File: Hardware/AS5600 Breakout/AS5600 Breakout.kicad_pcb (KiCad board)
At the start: 2 copper layers, 42.3 x 42.3 mm, 161 parts, among them J1 Conn_01x08, U1 AS5600

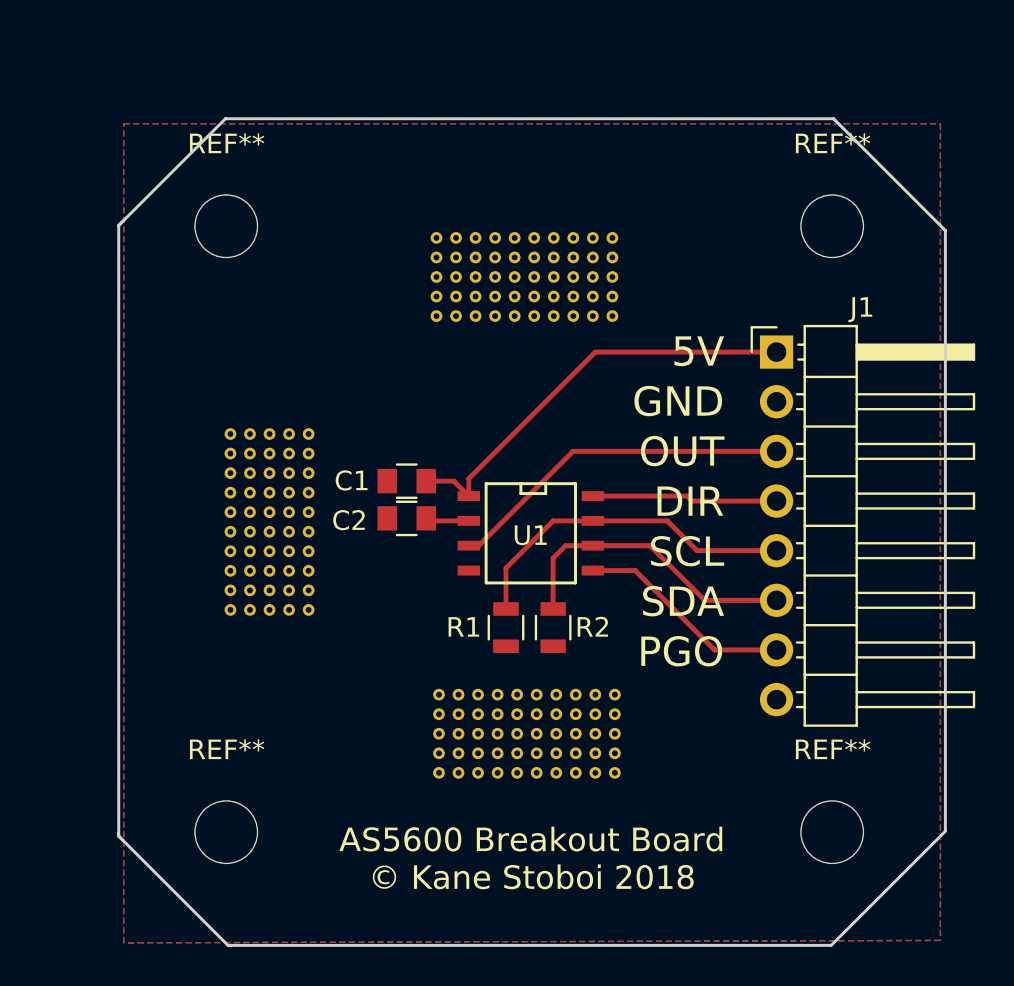
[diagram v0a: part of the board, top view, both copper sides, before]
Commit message: Completed breakout boards and BOM
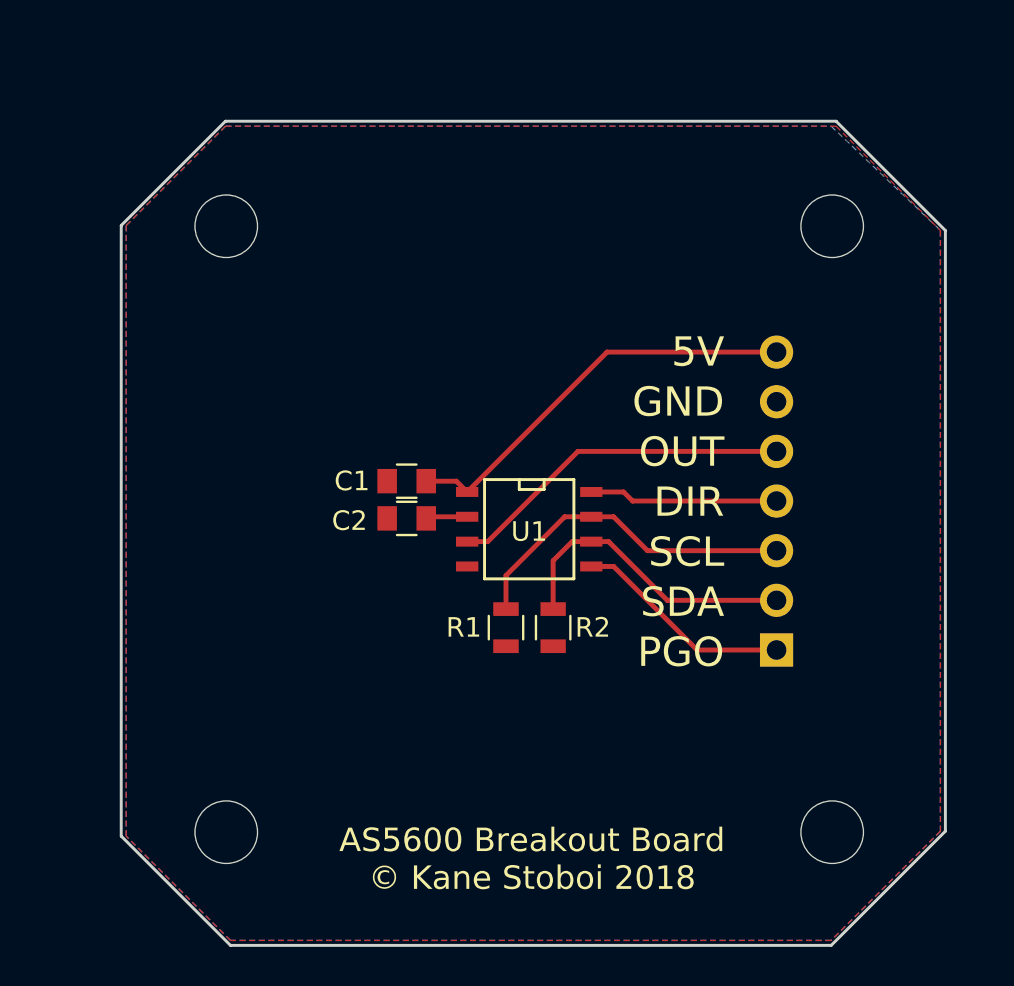
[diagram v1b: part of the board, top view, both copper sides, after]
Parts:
- removed the REF** at (145.4, 128.6)
- removed the REF** at (136.4, 128.6)
- removed the REF** at (144.3, 105.2)
- removed the REF** at (143.3, 105.2)
- removed the REF** at (142.3, 105.2)
- removed the REF** at (141.3, 105.2)
- removed the REF** at (140.3, 105.2)
- removed the REF** at (139.3, 105.2)
- removed the REF** at (138.3, 105.2)
- removed the REF** at (137.3, 105.2)
- removed the REF** at (136.3, 105.2)
- removed the REF** at (145.3, 104.2)
- removed the REF** at (145.4, 127.6)
- removed the REF** at (144.3, 104.2)
- removed the REF** at (143.3, 104.2)
- removed the REF** at (142.3, 104.2)
- removed the REF** at (141.3, 104.2)
- removed the REF** at (140.3, 104.2)
- removed the REF** at (139.3, 104.2)
- removed the REF** at (138.3, 104.2)
- removed the REF** at (137.3, 104.2)
- removed the REF** at (136.3, 104.2)
- removed the REF** at (145.3, 103.2)
- removed the REF** at (144.4, 127.6)
- removed the REF** at (144.3, 103.2)
- removed the REF** at (143.3, 103.2)
- removed the REF** at (142.3, 103.2)
- removed the REF** at (141.3, 103.2)
- removed the REF** at (140.3, 103.2)
- removed the REF** at (139.3, 103.2)
- removed the REF** at (138.3, 103.2)
- removed the REF** at (137.3, 103.2)
- removed the REF** at (136.3, 103.2)
- removed the REF** at (145.3, 102.2)
- removed the REF** at (143.4, 127.6)
- removed the REF** at (144.3, 102.2)
- removed the REF** at (143.3, 102.2)
- removed the REF** at (142.3, 102.2)
- removed the REF** at (141.3, 102.2)
- removed the REF** at (140.3, 102.2)
- removed the REF** at (139.3, 102.2)
- removed the REF** at (138.3, 102.2)
- removed the REF** at (137.3, 102.2)
- removed the REF** at (136.3, 102.2)
- removed the REF** at (145.3, 101.2)
- removed the REF** at (142.4, 127.6)
- removed the REF** at (144.3, 101.2)
- removed the REF** at (143.3, 101.2)
- removed the REF** at (142.3, 101.2)
- removed the REF** at (141.3, 101.2)
- removed the REF** at (140.3, 101.2)
- removed the REF** at (139.3, 101.2)
- removed the REF** at (138.3, 101.2)
- removed the REF** at (137.3, 101.2)
- removed the REF** at (141.4, 127.6)
- removed the REF** at (136.3, 101.2)
- removed the REF** at (125.7, 111.3)
- removed the REF** at (136.4, 124.6)
- removed the REF** at (140.4, 127.6)
- removed the REF** at (139.4, 127.6)
- removed the REF** at (138.4, 127.6)
- removed the REF** at (137.4, 127.6)
- removed the REF** at (144.4, 128.6)
- removed the REF** at (136.4, 127.6)
- removed the REF** at (145.4, 126.6)
- removed the REF** at (144.4, 126.6)
- removed the REF** at (143.4, 126.6)
- removed the REF** at (142.4, 126.6)
- removed the REF** at (141.4, 126.6)
- removed the REF** at (140.4, 126.6)
- removed the REF** at (139.4, 126.6)
- removed the REF** at (138.4, 126.6)
- removed the REF** at (137.4, 126.6)
- removed the REF** at (143.4, 128.6)
- removed the REF** at (136.4, 126.6)
- removed the REF** at (145.4, 125.6)
- removed the REF** at (144.4, 125.6)
- removed the REF** at (143.4, 125.6)
- removed the REF** at (142.4, 125.6)
- removed the REF** at (141.4, 125.6)
- removed the REF** at (140.4, 125.6)
- removed the REF** at (139.4, 125.6)
- removed the REF** at (138.4, 125.6)
- removed the REF** at (137.4, 125.6)
- removed the REF** at (142.4, 128.6)
- removed the REF** at (136.4, 125.6)
- removed the REF** at (145.4, 124.6)
- removed the REF** at (144.4, 124.6)
- removed the REF** at (143.4, 124.6)
- removed the REF** at (142.4, 124.6)
- removed the REF** at (141.4, 124.6)
- removed the REF** at (140.4, 124.6)
- removed the REF** at (139.4, 124.6)
- removed the REF** at (138.4, 124.6)
- removed the REF** at (137.4, 124.6)
- removed the REF** at (141.4, 128.6)
- removed the REF** at (129.7, 120.3)
- removed the REF** at (128.7, 120.3)
- removed the REF** at (127.7, 120.3)
- removed the REF** at (126.7, 120.3)
- removed the REF** at (125.7, 120.3)
- removed the REF** at (129.7, 119.3)
- removed the REF** at (128.7, 119.3)
- removed the REF** at (127.7, 119.3)
- removed the REF** at (126.7, 119.3)
- removed the REF** at (125.7, 119.3)
- removed the REF** at (140.4, 128.6)
- removed the REF** at (129.7, 118.3)
- removed the REF** at (128.7, 118.3)
- removed the REF** at (127.7, 118.3)
- removed the REF** at (126.7, 118.3)
- removed the REF** at (125.7, 118.3)
- removed the REF** at (129.7, 117.3)
- removed the REF** at (128.7, 117.3)
- removed the REF** at (127.7, 117.3)
- removed the REF** at (126.7, 117.3)
- removed the REF** at (125.7, 117.3)
- removed the REF** at (139.4, 128.6)
- removed the REF** at (129.7, 116.3)
- removed the REF** at (128.7, 116.3)
- removed the REF** at (127.7, 116.3)
- removed the REF** at (126.7, 116.3)
- removed the REF** at (125.7, 116.3)
- removed the REF** at (129.7, 115.3)
- removed the REF** at (128.7, 115.3)
- removed the REF** at (127.7, 115.3)
- removed the REF** at (126.7, 115.3)
- removed the REF** at (125.7, 115.3)
- removed the REF** at (138.4, 128.6)
- removed the REF** at (129.7, 114.3)
- removed the REF** at (128.7, 114.3)
- removed the REF** at (127.7, 114.3)
- removed the REF** at (126.7, 114.3)
- removed the REF** at (125.7, 114.3)
- removed the REF** at (129.7, 113.3)
- removed the REF** at (128.7, 113.3)
- removed the REF** at (127.7, 113.3)
- removed the REF** at (126.7, 113.3)
- removed the REF** at (125.7, 113.3)
- removed the REF** at (137.4, 128.6)
- removed the REF** at (129.7, 112.3)
- removed the REF** at (128.7, 112.3)
- removed the REF** at (127.7, 112.3)
- removed the REF** at (126.7, 112.3)
- removed the REF** at (125.7, 112.3)
- removed the REF** at (129.7, 111.3)
- removed the REF** at (128.7, 111.3)
- removed the REF** at (127.7, 111.3)
- removed the REF** at (126.7, 111.3)
- removed the REF** at (145.3, 105.2)
- ? (x4): renamed from REF**; value MountingHole_3.2mm_M3 -> (none)
- J1: value Conn_01x08 -> Conn_01x07; footprint Pin_Headers:Pin_Header_Angled_1x08_Pitch2.54mm -> Pin_Headers:Pin_Header_Angled_1x07_Pitch2.54mm; moved to B.Cu
- moved J1 15.2 mm to (153.7, 122.3)
- moved U1 0.22 mm to (141.0, 116.1)
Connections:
- J1 pad 1: 5V -> PGO
- J1 pad 2: GND -> SDA
- J1 pad 3: OUT -> SCL
- J1 pad 5: SCL -> OUT
- J1 pad 6: SDA -> GND
- J1 pad 7: PGO -> 5V
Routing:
- net 5V: track 21.8 -> 21.1 mm
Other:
- board size 42.3 x 42.3 mm -> 42.2 x 42.2 mm

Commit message: Created gerbers for pcbs
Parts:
- added REF**: VIA-0.6mm, VIAs:VIA-0.6mm, F.Cu at (137.5, 101.3)
- added REF**: VIA-0.6mm, VIAs:VIA-0.6mm, F.Cu at (135.0, 118.0)
- added REF**: VIA-0.6mm, VIAs:VIA-0.6mm, F.Cu at (135.0, 119.6)
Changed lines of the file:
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@@
 (kicad_pcb (version 4) (host pcbnew 4.0.7)
   (general
-    (links 15)
+    (links 18)
     (no_connects 0)
-    (area 120.066999 95.174999 162.381001 137.489001)
+    (area -4.438094 -2.499 164.445001 137.489001)
     (thickness 1.6)
     (drawings 24)
     (tracks 28)
     (zones 0)
-    (modules 11)
+    (modules 14)
     (nets 9)
   )
@@
   (layers
     (0 F.Cu signal)
-    (31 B.Cu signal hide)
+    (31 B.Cu signal)
     (32 B.Adhes user)
     (33 F.Adhes user)
@@
     (visible_elements 7FFEFF7F)
     (pcbplotparams
-      (layerselection 0x00030_80000001)
-      (usegerberextensions false)
+      (layerselection 0x010f0_80000001)
+      (usegerberextensions true)
       (excludeedgelayer true)
       (linewidth 0.100000)
@@
       (psa4output false)
       (plotreference true)
-      (plotvalue true)
+      (plotvalue false)
       (plotinvisibletext false)
       (padsonsilk false)
@@
       (outputformat 1)
       (mirror false)
-      (drillshape 1)
+      (drillshape 0)
       (scaleselection 1)
       (outputdirectory ""))
@@
     (add_net SCL)
     (add_net SDA)
+  )
+  (module VIAs:VIA-0.6mm (layer F.Cu)
+    (at 137.541 101.346)
+    (fp_text reference REF** (at 0 1.397) (layer F.SilkS) hide
+      (effects (font (size 1 1) (thickness 0.15)))
+    )
+    (fp_text value VIA-0.6mm (at 0 -1.524) (layer F.Fab) hide
+      (effects (font (size 1 1) (thickness 0.15)))
+    )
+    (pad 1 thru_hole circle (at 0 0) (size 0.6 0.6) (drill 0.3) (layers *.Cu)
+      (net 1 GND) (zone_connect 2))
+  )
+  (module VIAs:VIA-0.6mm (layer F.Cu)
+    (at 135.001 117.983)
+    (fp_text reference REF** (at 0 1.397) (layer F.SilkS) hide
+      (effects (font (size 1 1) (thickness 0.15)))
+    )
+    (fp_text value VIA-0.6mm (at 0 -1.524) (layer F.Fab) hide
+      (effects (font (size 1 1) (thickness 0.15)))
+    )
+    (pad 1 thru_hole circle (at 0 0) (size 0.6 0.6) (drill 0.3) (layers *.Cu)
+      (net 1 GND) (zone_connect 2))
   )
   (module VIA-0.6mm (layer F.Cu)
@@
     )
   )
+  (module VIAs:VIA-0.6mm (layer F.Cu)
+    (at 135.001 119.634)
+    (fp_text reference REF** (at 0 1.397) (layer F.SilkS) hide
+      (effects (font (size 1 1) (thickness 0.15)))
+    )
+    (fp_text value VIA-0.6mm (at 0 -1.524) (layer F.Fab) hide
+      (effects (font (size 1 1) (thickness 0.15)))
+    )
+    (pad 1 thru_hole circle (at 0 0) (size 0.6 0.6) (drill 0.3) (layers *.Cu)
+      (net 1 GND) (zone_connect 2))
+  )
   (gr_text "AS5600 Breakout Board\n© Kane Stoboi 2018" (at 141.165 133) (layer B.SilkS)
     (effects (font (size 1.2 1.2) (thickness 0.25)) (justify mirror))
@@
     (effects (font (size 1.5 1.5) (thickness 0.3)) (justify right))
   )
-  (segment (start 137.84 115.488) (end 135.829 115.488) (width 0.25) (layer F.Cu) (net 2) (status C00000))
-  (segment (start 135.829 115.488) (end 135.747 115.57) (width 0.25) (layer F.Cu) (net 2) (status C00000))
+  (segment (start 137.84 115.488) (end 135.829 115.488) (width 0.25) (layer F.Cu) (net 2))
+  (segment (start 135.829 115.488) (end 135.747 115.57) (width 0.25) (layer F.Cu) (net 2))
   (segment (start 135.874 115.697) (end 135.747 115.57) (width 0.25) (layer F.Cu) (net 2))
-  (segment (start 153.67 107.061) (end 144.997 107.061) (width 0.25) (layer F.Cu) (net 3) (status 400000))
-  (segment (start 144.997 107.061) (end 137.84 114.218) (width 0.25) (layer F.Cu) (net 3) (status 800000))
-  (segment (start 135.747 113.665) (end 137.287 113.665) (width 0.25) (layer F.Cu) (net 3) (status 400000))
-  (segment (start 137.287 113.665) (end 137.84 114.218) (width 0.25) (layer F.Cu) (net 3) (status 800000))
-  (segment (start 137.84 116.758) (end 138.893 116.758) (width 0.25) (layer F.Cu) (net 4) (status 400000))
-  (segment (start 143.51 112.141) (end 153.67 112.141) (width 0.25) (layer F.Cu) (net 4) (status 800000))
+  (segment (start 153.67 107.061) (end 144.997 107.061) (width 0.25) (layer F.Cu) (net 3))
+  (segment (start 144.997 107.061) (end 137.84 114.218) (width 0.25) (layer F.Cu) (net 3))
+  (segment (start 135.747 113.665) (end 137.287 113.665) (width 0.25) (layer F.Cu) (net 3))
+  (segment (start 137.287 113.665) (end 137.84 114.218) (width 0.25) (layer F.Cu) (net 3))
+  (segment (start 137.84 116.758) (end 138.893 116.758) (width 0.25) (layer F.Cu) (net 4))
+  (segment (start 143.51 112.141) (end 153.67 112.141) (width 0.25) (layer F.Cu) (net 4))
   (segment (start 138.893 116.758) (end 143.51 112.141) (width 0.25) (layer F.Cu) (net 4))
-  (segment (start 144.19 114.218) (end 145.841 114.218) (width 0.25) (layer F.Cu) (net 5) (status 400000))
-  (segment (start 146.304 114.681) (end 153.67 114.681) (width 0.25) (layer F.Cu) (net 5) (status 800000))
+  (segment (start 144.19 114.218) (end 145.841 114.218) (width 0.25) (layer F.Cu) (net 5))
+  (segment (start 146.304 114.681) (end 153.67 114.681) (width 0.25) (layer F.Cu) (net 5))
   (segment (start 145.841 114.218) (end 146.304 114.681) (width 0.25) (layer F.Cu) (net 5))
-  (segment (start 144.19 115.488) (end 142.83 115.488) (width 0.25) (layer F.Cu) (net 6) (status 400000))
-  (segment (start 139.827 118.491) (end 139.827 120.208) (width 0.25) (layer F.Cu) (net 6) (status 800000))
+  (segment (start 144.19 115.488) (end 142.83 115.488) (width 0.25) (layer F.Cu) (net 6))
+  (segment (start 139.827 118.491) (end 139.827 120.208) (width 0.25) (layer F.Cu) (net 6))
   (segment (start 142.83 115.488) (end 139.827 118.491) (width 0.25) (layer F.Cu) (net 6))
-  (segment (start 144.19 115.488) (end 145.333 115.488) (width 0.25) (layer F.Cu) (net 6) (status 400000))
-  (segment (start 147.066 117.221) (end 153.67 117.221) (width 0.25) (layer F.Cu) (net 6) (status 800000))
+  (segment (start 144.19 115.488) (end 145.333 115.488) (width 0.25) (layer F.Cu) (net 6))
+  (segment (start 147.066 117.221) (end 153.67 117.221) (width 0.25) (layer F.Cu) (net 6))
   (segment (start 145.333 115.488) (end 147.066 117.221) (width 0.25) (layer F.Cu) (net 6))
-  (segment (start 142.24 120.208) (end 142.24 117.729) (width 0.25) (layer F.Cu) (net 7) (status 400000))
-  (segment (start 143.211 116.758) (end 144.19 116.758) (width 0.25) (layer F.Cu) (net 7) (status 800000))
+  (segment (start 142.24 120.208) (end 142.24 117.729) (width 0.25) (layer F.Cu) (net 7))
+  (segment (start 143.211 116.758) (end 144.19 116.758) (width 0.25) (layer F.Cu) (net 7))
   (segment (start 142.24 117.729) (end 143.211 116.758) (width 0.25) (layer F.Cu) (net 7))
-  (segment (start 144.19 116.758) (end 145.079 116.758) (width 0.25) (layer F.Cu) (net 7) (status 400000))
-  (segment (start 148.082 119.761) (end 153.67 119.761) (width 0.25) (layer F.Cu) (net 7) (status 800000))
+  (segment (start 144.19 116.758) (end 145.079 116.758) (width 0.25) (layer F.Cu) (net 7))
+  (segment (start 148.082 119.761) (end 153.67 119.761) (width 0.25) (layer F.Cu) (net 7))
   (segment (start 145.079 116.758) (end 148.082 119.761) (width 0.25) (layer F.Cu) (net 7))
-  (segment (start 144.19 118.028) (end 145.333 118.028) (width 0.25) (layer F.Cu) (net 8) (status 400000))
-  (segment (start 149.606 122.301) (end 153.67 122.301) (width 0.25) (layer F.Cu) (net 8) (status 800000))
+  (segment (start 144.19 118.028) (end 145.333 118.028) (width 0.25) (layer F.Cu) (net 8))
+  (segment (start 149.606 122.301) (end 153.67 122.301) (width 0.25) (layer F.Cu) (net 8))
   (segment (start 145.333 118.028) (end 149.606 122.301) (width 0.25) (layer F.Cu) (net 8))
   (zone (net 1) (net_name GND) (layer F.Cu) (hatch edge 0.508)
